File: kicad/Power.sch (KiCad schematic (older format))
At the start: 14 parts, among them U2 7805, U3 TMR_3-1221

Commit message: Adding untracked files
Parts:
- removed C2: 0.33u, Capacitors_SMD:C_1206_HandSoldering, symbol C
- removed C3: 0.1u, Capacitors_SMD:C_1206_HandSoldering, symbol C
- removed U2: 7805, VB_7805:TO-220_Neutral123_Vertical_LargePads, symbol 7805
- renumbered C4 to C2, C5 to C3, C6 to C4, C7 to C5, C8 to C6, C9 to C7, C10 to C8, C11 to C9, U3 to U2
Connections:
- wire segments 17 -> 14
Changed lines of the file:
@@
 $EndDescr
 $Comp
-L C C2
-U 1 1 56CAF3D7
-P 5250 2650
-F 0 "C2" H 5275 2750 50  0000 L CNN
-F 1 "0.33u" H 5275 2550 50  0000 L CNN
-F 2 "Capacitors_SMD:C_1206_HandSoldering" H 5288 2500 50  0001 C CNN
-F 3 "" H 5250 2650 50  0000 C CNN
-	1    5250 2650
-	1    0    0    -1
-$EndComp
-$Comp
-L C C3
-U 1 1 56CAF408
-P 6050 2650
-F 0 "C3" H 6075 2750 50  0000 L CNN
-F 1 "0.1u" H 6075 2550 50  0000 L CNN
-F 2 "Capacitors_SMD:C_1206_HandSoldering" H 6088 2500 50  0001 C CNN
-F 3 "" H 6050 2650 50  0000 C CNN
-	1    6050 2650
-	1    0    0    -1
-$EndComp
-$Comp
-L GNDD #PWR011
-U 1 1 56CAF440
-P 5650 2800
-F 0 "#PWR011" H 5650 2550 50  0001 C CNN
-F 1 "GNDD" H 5650 2650 50  0000 C CNN
-F 2 "" H 5650 2800 50  0000 C CNN
-F 3 "" H 5650 2800 50  0000 C CNN
-	1    5650 2800
-	1    0    0    -1
-$EndComp
-$Comp
-L +12V #PWR012
-U 1 1 56CAF46E
-P 4650 2500
-F 0 "#PWR012" H 4650 2350 50  0001 C CNN
-F 1 "+12V" H 4650 2640 50  0000 C CNN
-F 2 "" H 4650 2500 50  0000 C CNN
-F 3 "" H 4650 2500 50  0000 C CNN
-	1    4650 2500
-	1    0    0    -1
-$EndComp
-$Comp
-L +5VD #PWR013
-U 1 1 56CAF4A2
-P 6650 2500
-F 0 "#PWR013" H 6650 2350 50  0001 C CNN
-F 1 "+5VD" H 6650 2640 50  0000 C CNN
-F 2 "" H 6650 2500 50  0000 C CNN
-F 3 "" H 6650 2500 50  0000 C CNN
-	1    6650 2500
-	1    0    0    -1
-$EndComp
-$Comp
-L TMR_3-1221 U3
+L TMR_3-1221 U2
 U 1 1 56CB02BD
 P 6000 4500
-F 0 "U3" H 6000 3600 60  0000 C CNN
+F 0 "U2" H 6000 3600 60  0000 C CNN
 F 1 "TMR_3-1221" H 6000 4500 60  0000 C CNN
 F 2 "TracoPower:TMR_3" H 6000 4500 60  0001 C CNN
@@
 $EndComp
 $Comp
-L GNDD #PWR014
+L GNDD #PWR013
 U 1 1 56CB031C
 P 4450 5250
-F 0 "#PWR014" H 4450 5000 50  0001 C CNN
+F 0 "#PWR013" H 4450 5000 50  0001 C CNN
 F 1 "GNDD" H 4450 5100 50  0000 C CNN
 F 2 "" H 4450 5250 50  0000 C CNN
@@
 $EndComp
 $Comp
-L +12V #PWR015
+L +12V #PWR014
 U 1 1 56CB0338
 P 4450 4650
-F 0 "#PWR015" H 4450 4500 50  0001 C CNN
+F 0 "#PWR014" H 4450 4500 50  0001 C CNN
 F 1 "+12V" H 4450 4790 50  0000 C CNN
 F 2 "" H 4450 4650 50  0000 C CNN
@@
 $EndComp
 $Comp
-L GNDA #PWR016
+L GNDA #PWR015
 U 1 1 56CB035C
 P 6550 5450
-F 0 "#PWR016" H 6550 5200 50  0001 C CNN
+F 0 "#PWR015" H 6550 5200 50  0001 C CNN
 F 1 "GNDA" H 6550 5300 50  0000 C CNN
 F 2 "" H 6550 5450 50  0000 C CNN
@@
 $EndComp
 $Comp
-L +5VA #PWR017
+L +5VA #PWR016
 U 1 1 56CB07D6
 P 7050 4950
-F 0 "#PWR017" H 7050 4800 50  0001 C CNN
+F 0 "#PWR016" H 7050 4800 50  0001 C CNN
 F 1 "+5VA" H 7050 5090 50  0000 C CNN
 F 2 "" H 7050 4950 50  0000 C CNN
@@
 $EndComp
 $Comp
-L -5VA #PWR16
+L -5VA #PWR14
 U 1 1 56CB07F6
 P 7050 5150
-F 0 "#PWR16" H 7050 5250 50  0001 C CNN
+F 0 "#PWR14" H 7050 5250 50  0001 C CNN
 F 1 "-5VA" H 7050 5300 50  0000 C CNN
 F 2 "" H 7050 5150 50  0000 C CNN
@@
 $EndComp
 Wire Wire Line
-	5250 2800 6050 2800
-Connection ~ 5650 2800
-Wire Wire Line
-	6050 2500 6650 2500
-Wire Wire Line
-	5250 2500 4650 2500
-Wire Wire Line
 	4450 4650 4850 4650
 Wire Wire Line
@@
 	5450 4650 5650 4650
 $Comp
-L PWR_FLAG #FLG018
+L PWR_FLAG #FLG017
 U 1 1 56CB7727
 P 5450 4650
-F 0 "#FLG018" H 5450 4745 50  0001 C CNN
+F 0 "#FLG017" H 5450 4745 50  0001 C CNN
 F 1 "PWR_FLAG" H 5450 4830 50  0000 C CNN
 F 2 "" H 5450 4650 50  0000 C CNN
@@
 $EndComp
 $Comp
-L C C5
+L C C3
 U 1 1 56CB79FB
 P 8800 4850
-F 0 "C5" H 8825 4950 50  0000 L CNN
+F 0 "C3" H 8825 4950 50  0000 L CNN
 F 1 "0.1u" H 8825 4750 50  0000 L CNN
 F 2 "Capacitors_SMD:C_1206_HandSoldering" H 8838 4700 50  0001 C CNN
@@
 $EndComp
 $Comp
-L C C6
+L C C4
 U 1 1 56CB7A4E
 P 8800 5150
-F 0 "C6" H 8825 5250 50  0000 L CNN
+F 0 "C4" H 8825 5250 50  0000 L CNN
 F 1 "0.1u" H 8825 5050 50  0000 L CNN
 F 2 "Capacitors_SMD:C_1206_HandSoldering" H 8838 5000 50  0001 C CNN
@@
 $EndComp
 $Comp
-L C C8
+L C C6
 U 1 1 56CB7A88
 P 9250 4850
-F 0 "C8" H 9275 4950 50  0000 L CNN
+F 0 "C6" H 9275 4950 50  0000 L CNN
 F 1 "0.1u" H 9275 4750 50  0000 L CNN
 F 2 "Capacitors_SMD:C_1206_HandSoldering" H 9288 4700 50  0001 C CNN
@@
 $EndComp
 $Comp
-L C C9
+L C C7
 U 1 1 56CB7AC1
 P 9250 5150
-F 0 "C9" H 9275 5250 50  0000 L CNN
+F 0 "C7" H 9275 5250 50  0000 L CNN
 F 1 "0.1u" H 9275 5050 50  0000 L CNN
 F 2 "Capacitors_SMD:C_1206_HandSoldering" H 9288 5000 50  0001 C CNN
@@
 $EndComp
 $Comp
-L C C10
+L C C8
 U 1 1 56CB7B1C
 P 9700 4850
-F 0 "C10" H 9725 4950 50  0000 L CNN
+F 0 "C8" H 9725 4950 50  0000 L CNN
 F 1 "0.1u" H 9725 4750 50  0000 L CNN
 F 2 "Capacitors_SMD:C_1206_HandSoldering" H 9738 4700 50  0001 C CNN
@@
 $EndComp
 $Comp
-L C C11
+L C C9
 U 1 1 56CB7B52
 P 9700 5150
-F 0 "C11" H 9725 5250 50  0000 L CNN
+F 0 "C9" H 9725 5250 50  0000 L CNN
 F 1 "0.1u" H 9725 5050 50  0000 L CNN
 F 2 "Capacitors_SMD:C_1206_HandSoldering" H 9738 5000 50  0001 C CNN
@@
 Connection ~ 9700 5300
 $Comp
-L GNDA #PWR019
+L GNDA #PWR018
 U 1 1 56CB7D48
 P 10300 5000
-F 0 "#PWR019" H 10300 4750 50  0001 C CNN
+F 0 "#PWR018" H 10300 4750 50  0001 C CNN
 F 1 "GNDA" H 10300 4850 50  0000 C CNN
 F 2 "" H 10300 5000 50  0000 C CNN
@@
 $EndComp
 $Comp
-L +5VA #PWR020
+L +5VA #PWR019
 U 1 1 56CB7D80
 P 10300 4700
-F 0 "#PWR020" H 10300 4550 50  0001 C CNN
+F 0 "#PWR019" H 10300 4550 50  0001 C CNN
 F 1 "+5VA" H 10300 4840 50  0000 C CNN
 F 2 "" H 10300 4700 50  0000 C CNN
@@
 $EndComp
 $Comp
-L -5VA #PWR21
+L -5VA #PWR19
 U 1 1 56CB7DB8
 P 10300 5300
-F 0 "#PWR21" H 10300 5400 50  0001 C CNN
+F 0 "#PWR19" H 10300 5400 50  0001 C CNN
 F 1 "-5VA" H 10300 5450 50  0000 C CNN
 F 2 "" H 10300 5300 50  0000 C CNN
@@
 $EndComp
 $Comp
-L C C4
+L C C2
 U 1 1 56CB7F0E
 P 8700 2650
-F 0 "C4" H 8725 2750 50  0000 L CNN
+F 0 "C2" H 8725 2750 50  0000 L CNN
 F 1 "0.1u" H 8725 2550 50  0000 L CNN
 F 2 "Capacitors_SMD:C_1206_HandSoldering" H 8738 2500 50  0001 C CNN
@@
 $EndComp
 $Comp
-L C C7
+L C C5
 U 1 1 56CB7F8E
 P 9150 2650
-F 0 "C7" H 9175 2750 50  0000 L CNN
+F 0 "C5" H 9175 2750 50  0000 L CNN
 F 1 "1u" H 9175 2550 50  0000 L CNN
 F 2 "Capacitors_SMD:C_1206_HandSoldering" H 9188 2500 50  0001 C CNN
@@
 $EndComp
 $Comp
-L +5VD #PWR021
+L +5VD #PWR020
 U 1 1 56CB800B
 P 9600 2500
-F 0 "#PWR021" H 9600 2350 50  0001 C CNN
+F 0 "#PWR020" H 9600 2350 50  0001 C CNN
 F 1 "+5VD" H 9600 2640 50  0000 C CNN
 F 2 "" H 9600 2500 50  0000 C CNN
@@
 $EndComp
 $Comp
-L GNDD #PWR022
+L GNDD #PWR021
 U 1 1 56CB8049
 P 9600 2800
-F 0 "#PWR022" H 9600 2550 50  0001 C CNN
+F 0 "#PWR021" H 9600 2550 50  0001 C CNN
 F 1 "GNDD" H 9600 2650 50  0000 C CNN
 F 2 "" H 9600 2800 50  0000 C CNN
@@
 	8700 2800 9600 2800
 Connection ~ 9150 2800
-$Comp
-L 7805 U2
-U 1 1 56CB9239
-P 5650 2550
-F 0 "U2" H 5800 2354 50  0000 C CNN
-F 1 "7805" H 5650 2750 50  0000 C CNN
-F 2 "VB_7805:TO-220_Neutral123_Vertical_LargePads" H 5650 2550 50  0001 C CNN
-F 3 "" H 5650 2550 50  0000 C CNN
-	1    5650 2550
-	1    0    0    -1
-$EndComp
 $EndSCHEMATC

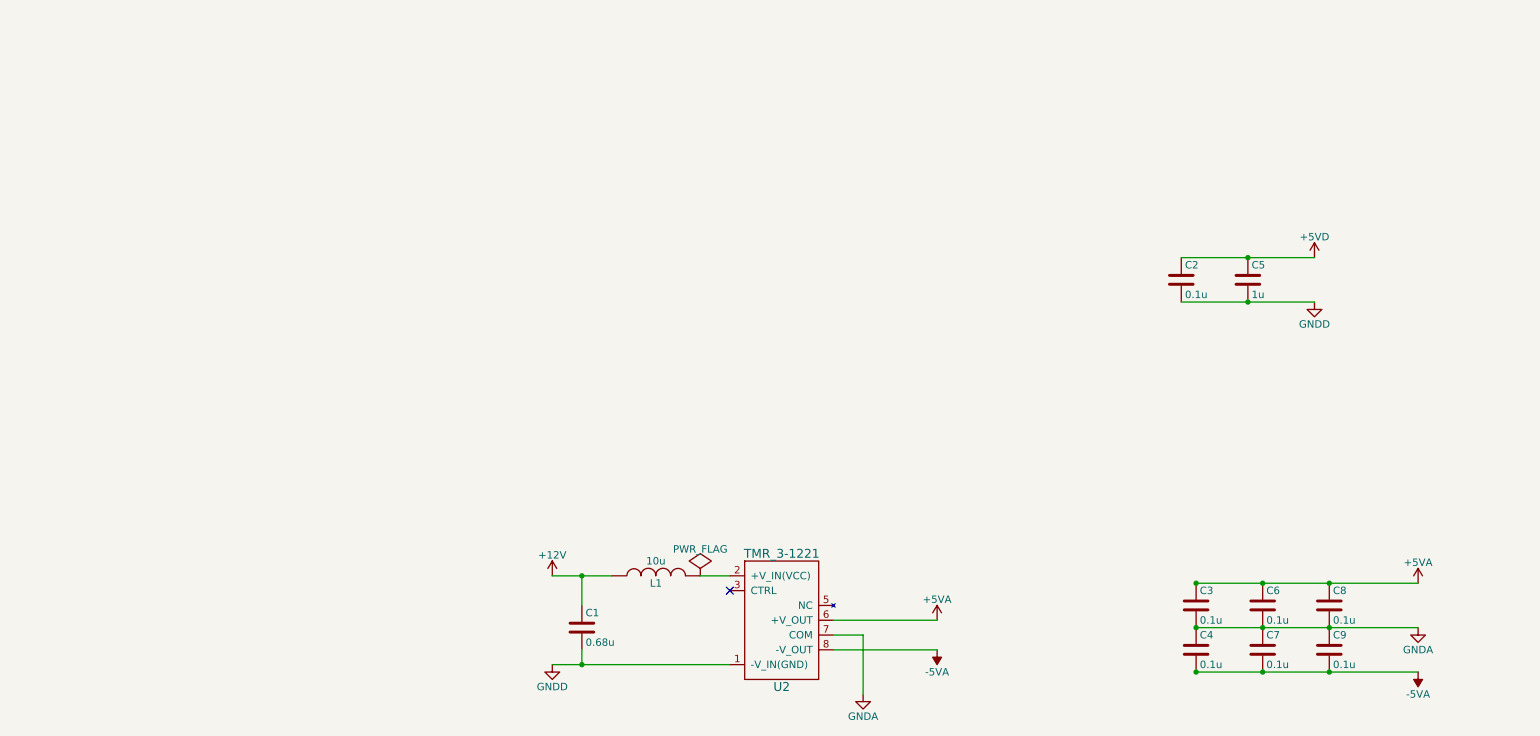
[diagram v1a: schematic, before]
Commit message: Reworked schematics to allow control of the power and introduction of ATMega328P for control
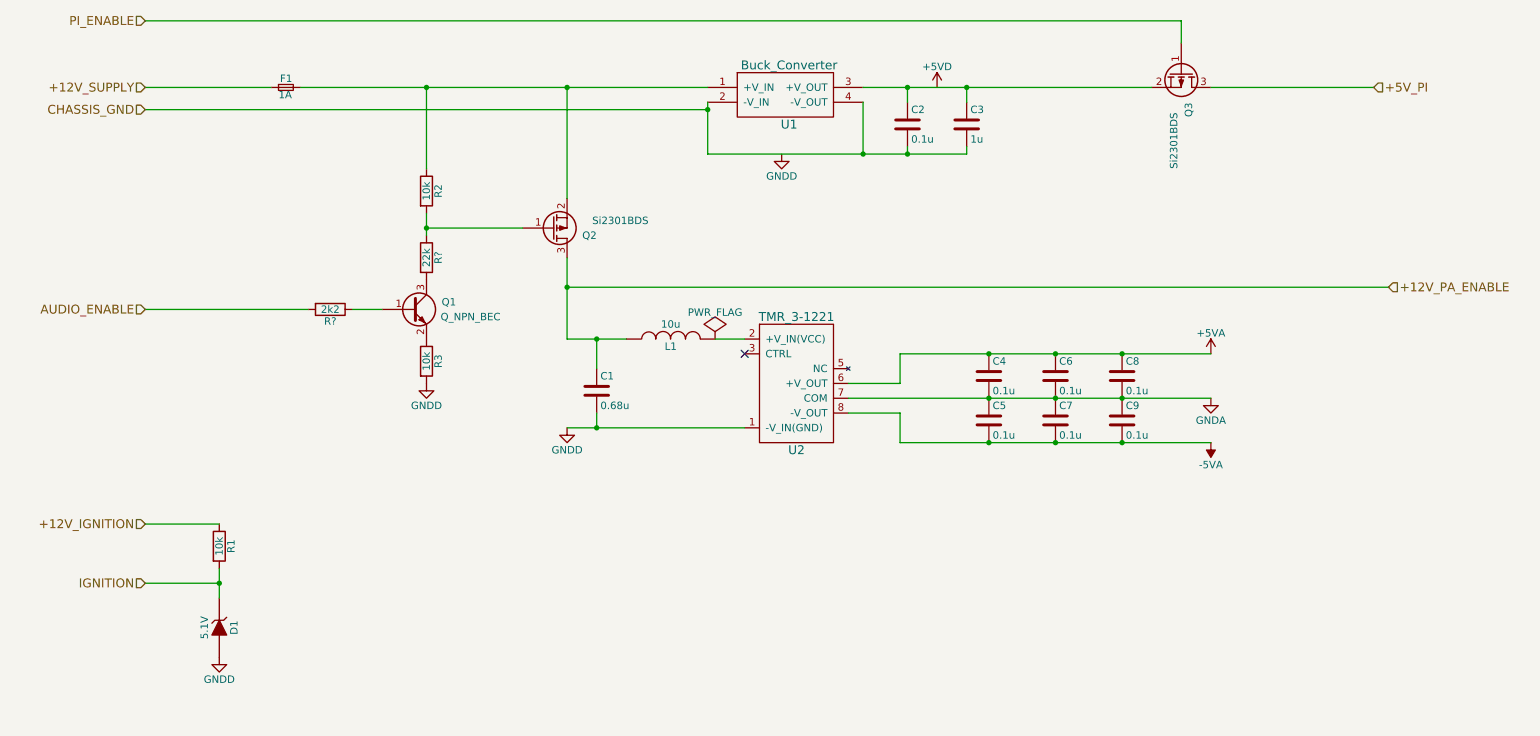
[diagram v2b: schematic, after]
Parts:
- added D1: 5.1V, symbol ZENER
- added F1: 1A, symbol F_Small
- added Q1: Q_NPN_BEC, symbol Q_NPN_BEC
- added Q2, Q3: Si2301BDS, symbol Q_PMOS_GSD
- added R1, R2, R3: 10k, symbol R
- added R?: 22k, symbol R
- added R?: 2k2, symbol R
- added U1: Buck_Converter, symbol Buck_Converter
- renumbered C5 to C3, C3 to C4, C4 to C5
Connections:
- net +5VD: no longer C2.1, C3.1
- net GNDD: now also D1.2 (A), R3.2; no longer C2.2, C3.2
- net +12V renamed +12V_PA_ENABLE
- net +12V_PA_ENABLE: now also Q2.3 (D)
- new net: C2.1, C3.1, Q3.2 (S), U1.3 (+V_OUT)
- new net: F1.2, Q2.2 (S), R2.1, U1.1 (+V_IN)
- new net: Q2.1 (G), R2.2, R?.1
- new net: Q1.2 (E), R3.1
- new net: Q1.1 (B), R?.1
- new net: Q1.3 (C), R?.2
- new net +12V_IGNITION: R1.1
- new net +12V_SUPPLY: F1.1
- new net +5V_PI: Q3.3 (D)
- new net AUDIO_ENABLE: R?.2
- new net CHASSIS_GND: C2.2, C3.2, U1.2 (-V_IN), U1.4 (-V_OUT)
- new net IGNITION: D1.1 (K), R1.2
- new net PI_ENABLE: Q3.1 (G)
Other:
- moved on the sheet: C1, C2, C3, C4, C5, C6, C7, C8, C9, L1, U2

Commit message: Produced Volume knob including Gerbers, and updated main board to remove ERC errors.  Just about to start board layout
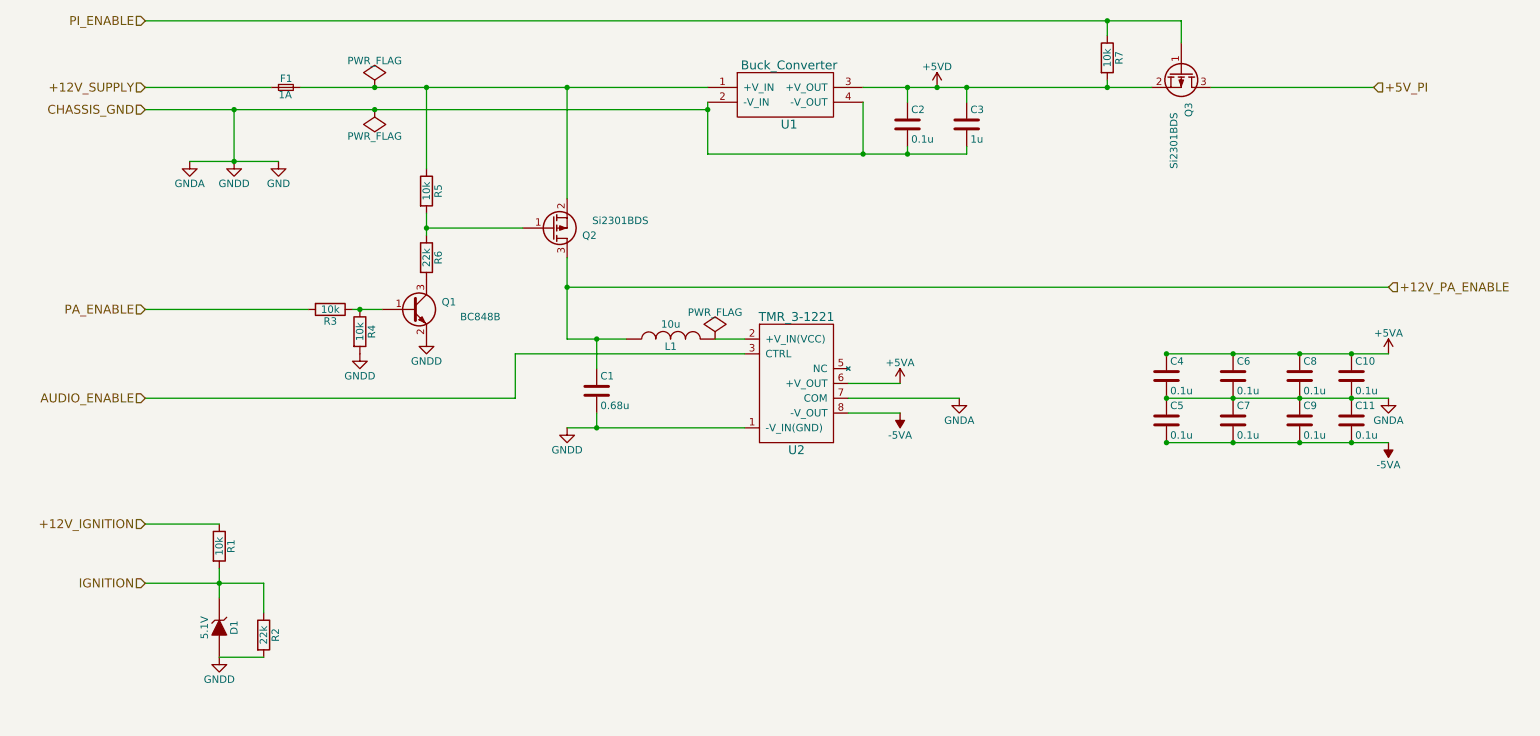
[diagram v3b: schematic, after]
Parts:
- removed R3: 10k, symbol R
- added C10, C11: 0.1u, Capacitors_SMD:C_0603_HandSoldering, symbol C
- added R2: 22k, Resistors_SMD:R_0603_HandSoldering, symbol R
- added R4, R7: 10k, Resistors_SMD:R_0603_HandSoldering, symbol R
- C2, C4, C5, C6, C7, C8, C9: footprint Capacitors_SMD:C_1206_HandSoldering -> Capacitors_SMD:C_0603_HandSoldering
- D1: footprint (none) -> Diodes_SMD:SOD-123
- F1: footprint (none) -> Fuse_Holders_and_Fuses:Fuseholder5x20_horiz_SemiClosed_Casing10x25mm
- Q1: value Q_NPN_BEC -> BC848B; footprint (none) -> TO_SOT_Packages_SMD:SOT-23_Handsoldering
- Q2, Q3: footprint (none) -> TO_SOT_Packages_SMD:SOT-23_Handsoldering
- R1: footprint (none) -> Resistors_SMD:R_0603_HandSoldering
- R3: renamed from R?; value 2k2 -> 10k; footprint (none) -> Resistors_SMD:R_0603_HandSoldering
- R5: renamed from R2; footprint (none) -> Resistors_SMD:R_0603_HandSoldering
- R6: renamed from R?; footprint (none) -> Resistors_SMD:R_0603_HandSoldering
- U1: footprint (none) -> Buck_Converter:Buck_Converter
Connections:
- net CHASSIS_GND is gone; now on net GND: C2.2, C3.2, U1.2 (-V_IN), U1.4 (-V_OUT)
- net GNDA is gone; now on net GND: C4.2, C5.1, C6.2, C7.1, C8.2, C9.1, U2.7 (COM)
- net GNDD is gone; now on net GND: C1.2, D1.2 (A), U2.1 (-V_IN(GND))
- net +5VA: now also C10.1
- net +5VD: now also C2.1, C3.1, Q3.2 (S), U1.3 (+V_OUT), R7.2
- net -5VA: now also C11.2
- net AUDIO_ENABLE: now also U2.3 (CTRL); no longer R3.2
- net IGNITION: now also R2.1
- net PI_ENABLE: now also R7.1
- net GND: now reaches Q1.2 (E)
- net GND: now also C10.2, C11.1, R2.2, R4.2
- net at Q1.1 (B), R3.1: now also R4.1
- new net PA_ENABLE: R3.2
- no-connect marks 1 -> 0
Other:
- moved on the sheet: C4, C5, C6, C7, C8, C9

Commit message: Routed the board.  Passes ERC check
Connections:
- net +12V_PA_ENABLE: no longer C1.1, L1.1
- net at F1.2, Q2.2 (S), R5.1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: now also C1.1, L1.1
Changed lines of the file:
@@
 $EndComp
-Wire Wire Line
-	4550 3050 4950 3050
 Wire Wire Line
 	4550 3650 5750 3650
@@
 Connection ~ 4750 3650
 Wire Wire Line
-	4750 3250 4750 3050
+	4750 1350 4750 3250
 Connection ~ 4750 3050
 Wire Wire Line
@@
 $EndComp
 Wire Wire Line
-	4550 2500 4550 3050
-Wire Wire Line
-	10100 2700 4550 2700
-Connection ~ 4550 2700
-Wire Wire Line
 	1700 900  8700 900
 Wire Wire Line
@@
 Wire Wire Line
 	4200 3150 5750 3150
+Wire Wire Line
+	4550 2500 4550 2700
+Wire Wire Line
+	4550 2700 10100 2700
+Wire Wire Line
+	4750 3050 4950 3050
+Connection ~ 4750 1350
 $EndSCHEMATC
